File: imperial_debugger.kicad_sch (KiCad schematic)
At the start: 0 parts

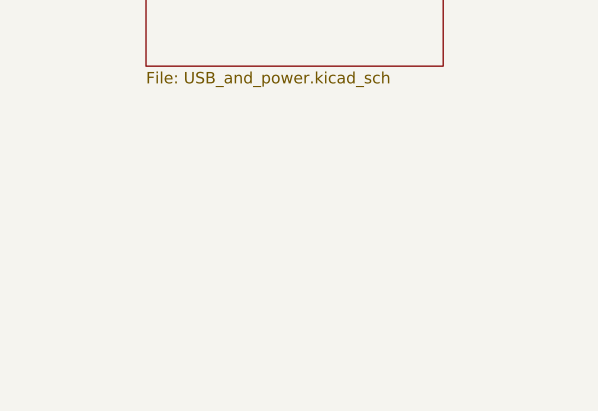
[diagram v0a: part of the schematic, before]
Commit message: After update to kicak 9.0
Signed-off-by: Marc Kelly <mpkelly@achenar.co.uk>
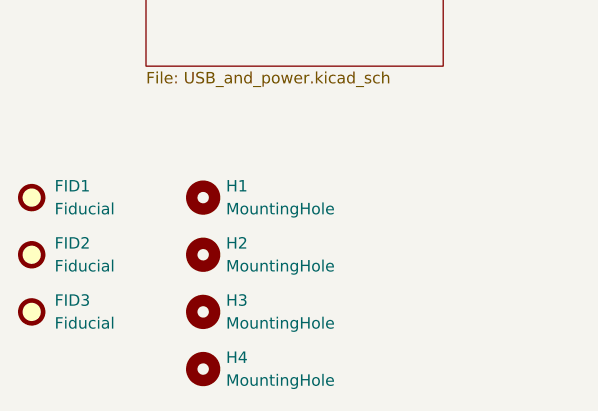
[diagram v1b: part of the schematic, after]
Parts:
- added FID1, FID2, FID3: Fiducial, Fiducial:Fiducial_1.5mm_Mask3mm, symbol Mechanical:Fiducial
- added H1, H2, H3, H4: MountingHole, MountingHole:MountingHole_3.2mm_M3, symbol Mechanical:MountingHole

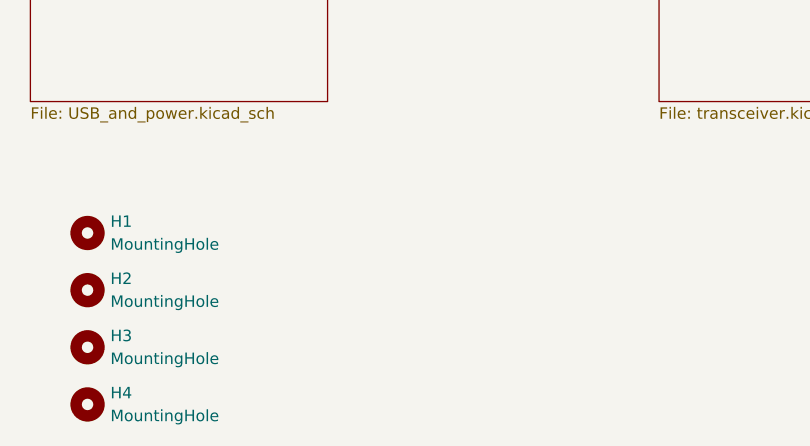
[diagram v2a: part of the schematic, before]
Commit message: Updated with the new design.
Removed all level translators.
4 sockets, 2x6 pin outputs
New PCB shape and routing
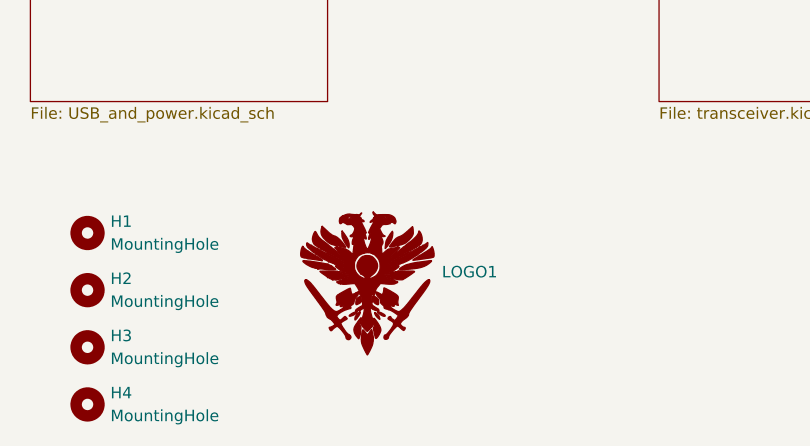
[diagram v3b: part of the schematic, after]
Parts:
- added LOGO1: ~, Achenar_Logos:achenar_logo, symbol logos:Achenar_Logo

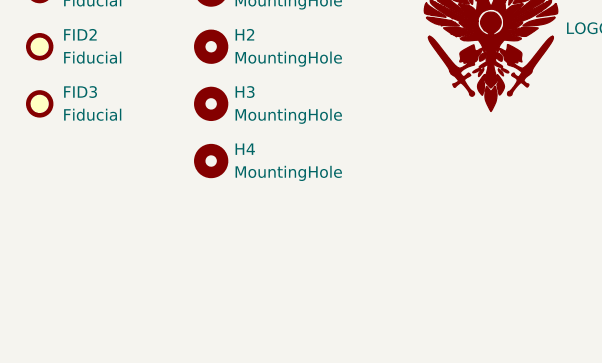
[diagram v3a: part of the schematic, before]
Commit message: Update schematics after moving to KiCad 10
Added some footprints to a local lib, as the silkscreen caused issues.

Signed-off-by: Marc Kelly <mpkelly@achenar.co.uk>
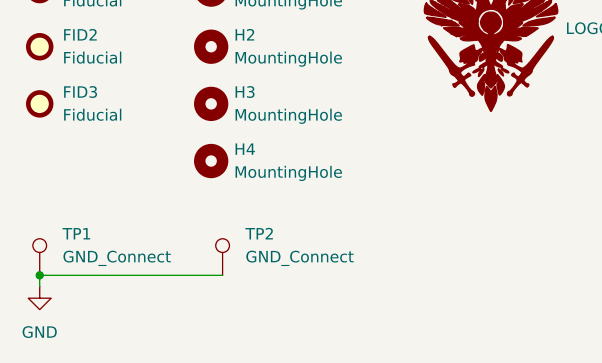
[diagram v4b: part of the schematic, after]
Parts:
- added TP1, TP2: GND_Connect, TestPoint:TestPoint_Keystone_5000-5004_Miniature, symbol Connector:TestPoint
- LOGO1: value ~ -> (none)
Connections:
- new net GND: TP1.1, TP2.1

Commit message: Sorting out BOMs
Signed-off-by: Marc Kelly <mpkelly@achenar.co.uk>
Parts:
- FID1, FID2, FID3, H1, H2, H3, H4: now left out of the parts list
- TP1: MFN (none) -> Keystone Electronics; MFP (none) -> 5006; SUPPLIER (none) -> Mouser; SUPPLIER_LINK (none) -> https://www.mouser.co.uk/ProductDetail/Keystone-Electronics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; SUPPLIER_PN (none) -> 534-5006
- TP2: MFN (none) -> Keystone Electronics; MFP (none) -> 5006; SUPPLIER (none) -> Mouser; SUPPLIER_PN (none) -> 534-5006
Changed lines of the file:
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@@
 		(body_style 1)
 		(exclude_from_sim no)
-		(in_bom yes)
+		(in_bom no)
 		(on_board yes)
 		(in_pos_files yes)
@@
 			)
 		)
-		(property "MFN" ""
+		(property "MFN" "Keystone Electronics"
 			(at 38.1 114.3 0)
 			(hide yes)
@@
 			)
 		)
-		(property "MFP" ""
+		(property "MFP" "5006"
 			(at 38.1 114.3 0)
 			(hide yes)
@@
 			)
 		)
-		(property "SUPPLIER" ""
+		(property "SUPPLIER" "Mouser"
 			(at 38.1 114.3 0)
 			(hide yes)
@@
 			)
 		)
-		(property "SUPPLIER_PN" ""
+		(property "SUPPLIER_PN" "534-5006"
 			(at 38.1 114.3 0)
 			(hide yes)
@@
 			)
 		)
-		(property "SUPPLIER_LINK" ""
+		(property "SUPPLIER_LINK" "https://www.mouser.co.uk/ProductDetail/Keystone-Electronics/5001?qs=q0tsjPZWdm%2FW0vdr%2FwowKg%3D%3D"
 			(at 38.1 114.3 0)
 			(hide yes)
@@
 			)
 		)
-		(property "MFN" ""
+		(property "MFN" "Keystone Electronics"
 			(at 58.42 114.3 0)
 			(hide yes)
@@
 			)
 		)
-		(property "MFP" ""
+		(property "MFP" "5006"
 			(at 58.42 114.3 0)
 			(hide yes)
@@
 			)
 		)
-		(property "SUPPLIER" ""
+		(property "SUPPLIER" "Mouser"
 			(at 58.42 114.3 0)
 			(hide yes)
@@
 			)
 		)
-		(property "SUPPLIER_PN" ""
+		(property "SUPPLIER_PN" "534-5006"
 			(at 58.42 114.3 0)
 			(hide yes)
@@
 		(body_style 1)
 		(exclude_from_sim no)
-		(in_bom yes)
+		(in_bom no)
 		(on_board yes)
 		(in_pos_files yes)
@@
 		(body_style 1)
 		(exclude_from_sim no)
-		(in_bom yes)
+		(in_bom no)
 		(on_board yes)
 		(in_pos_files yes)
@@
 		(body_style 1)
 		(exclude_from_sim no)
-		(in_bom yes)
+		(in_bom no)
 		(on_board yes)
 		(in_pos_files yes)
@@
 		(body_style 1)
 		(exclude_from_sim no)
-		(in_bom yes)
+		(in_bom no)
 		(on_board yes)
 		(in_pos_files yes)
@@
 		(body_style 1)
 		(exclude_from_sim no)
-		(in_bom yes)
+		(in_bom no)
 		(on_board yes)
 		(in_pos_files yes)
@@
 		(body_style 1)
 		(exclude_from_sim no)
-		(in_bom yes)
-		(on_board yes)
-		(in_pos_files yes)
+		(in_bom no)
+		(on_board yes)
+		(in_pos_files yes)
